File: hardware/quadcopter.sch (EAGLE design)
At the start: 55 parts, among them J1 HEADER-4POS-0.1IN-FEMALE-SMD-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, J2 HEADER-10POSTH-254X10, J3 HEADER-4POS-0.1IN-FEMALE, J4 AVR_SPI_PRG_6-SMD, M1 MOTOR_PADS_GND-MOLEX-SMD, M2 MOTOR_PADS_GND-MOLEX-SMD, M3 MOTOR_PADS_GND-MOLEX-SMD, M4 MOTOR_PADS_GND-MOLEX-SMD, Q1 N-MOSFET-SI2302DS, Q2 N-MOSFET-SI2302DS, Q3 N-MOSFET-SI2302DS, Q4 N-MOSFET-SI2302DS, SW1 PUSHBUTTON_-4.5X4.5, U1 ATMEGA128RFA1, U2 IMU_LSM9DS1-LSM9DS1, Y1 CRYSTAL5X3

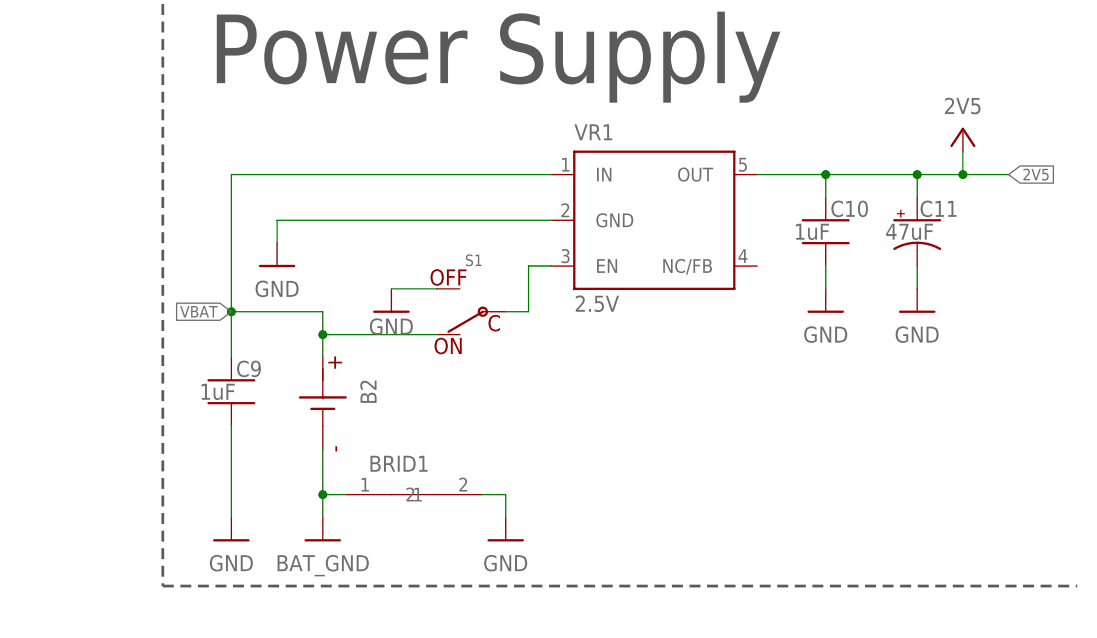
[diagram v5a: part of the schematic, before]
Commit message: Attempt to fix power supply to pass quick check
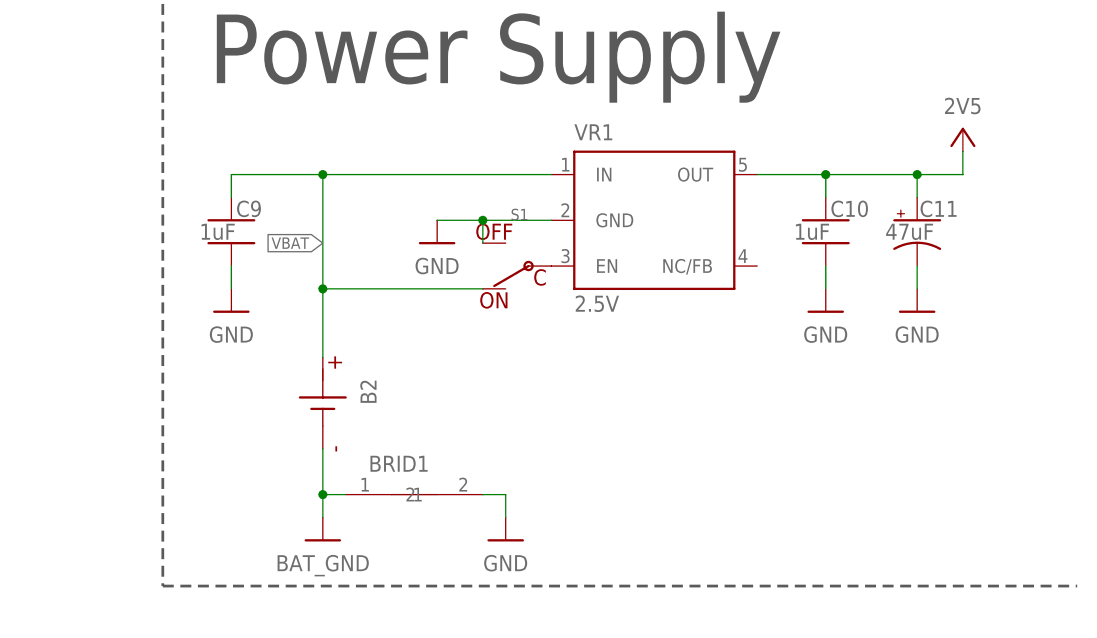
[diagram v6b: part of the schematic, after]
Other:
- moved on the sheet: C9, S1
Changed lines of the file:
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@@
 <part name="C10" library="quadparts_prebuilt_2022" library_urn="urn:adsk.wipprod:fs.file:vf.VudH_-qgS-enOFMGlZoxrw" deviceset="CAPACITOR-NP_" device="SMD-2012-0805_CERAMIC-1UF" value="1uF"/>
 <part name="S1" library="quadparts_prebuilt_2022" library_urn="urn:adsk.wipprod:fs.file:vf.VudH_-qgS-enOFMGlZoxrw" deviceset="POWER-SWITCH-MFS201N-9-Z" device="-SMD-EDGE"/>
-<part name="GND28" library="quadparts_prebuilt_2022" library_urn="urn:adsk.wipprod:fs.file:vf.VudH_-qgS-enOFMGlZoxrw" deviceset="GND" device=""/>
 <part name="GND31" library="quadparts_prebuilt_2022" library_urn="urn:adsk.wipprod:fs.file:vf.VudH_-qgS-enOFMGlZoxrw" deviceset="GND" device=""/>
 <part name="GND33" library="quadparts_prebuilt_2022" library_urn="urn:adsk.wipprod:fs.file:vf.VudH_-qgS-enOFMGlZoxrw" deviceset="GND" device=""/>
@@
 <attribute name="NAME" x="373.38" y="110.49" size="1.778" layer="95"/>
 </instance>
-<instance part="GND27" gate="1" x="340.36" y="96.52" smashed="yes">
-<attribute name="VALUE" x="340.36" y="93.98" size="1.778" layer="96" align="center"/>
-</instance>
-<instance part="C9" gate="G$1" x="335.28" y="83.82" smashed="yes">
-<attribute name="VALUE" x="331.724" y="81.661" size="1.778" layer="96"/>
-<attribute name="NAME" x="335.788" y="84.201" size="1.778" layer="95"/>
+<instance part="GND27" gate="1" x="358.14" y="99.06" smashed="yes">
+<attribute name="VALUE" x="358.14" y="96.52" size="1.778" layer="96" align="center"/>
+</instance>
+<instance part="C9" gate="G$1" x="335.28" y="101.6" smashed="yes">
+<attribute name="VALUE" x="331.724" y="99.441" size="1.778" layer="96"/>
+<attribute name="NAME" x="335.788" y="101.981" size="1.778" layer="95"/>
 </instance>
 <instance part="C10" gate="G$1" x="401.32" y="101.6" smashed="yes">
@@
 <attribute name="NAME" x="401.828" y="101.981" size="1.778" layer="95"/>
 </instance>
-<instance part="S1" gate="G$1" x="360.68" y="91.44" smashed="yes" rot="R180">
-<attribute name="NAME" x="363.22" y="97.79" size="1.27" layer="95" rot="R180"/>
-</instance>
-<instance part="GND28" gate="1" x="353.06" y="91.44" smashed="yes">
-<attribute name="VALUE" x="353.06" y="88.9" size="1.778" layer="96" align="bottom-center"/>
-</instance>
-<instance part="GND31" gate="1" x="335.28" y="66.04" smashed="yes">
-<attribute name="VALUE" x="335.28" y="63.5" size="1.778" layer="96" align="center"/>
+<instance part="S1" gate="G$1" x="365.76" y="96.52" smashed="yes" rot="R180">
+<attribute name="NAME" x="368.3" y="102.87" size="1.27" layer="95" rot="R180"/>
+</instance>
+<instance part="GND31" gate="1" x="335.28" y="91.44" smashed="yes">
+<attribute name="VALUE" x="335.28" y="88.9" size="1.778" layer="96" align="center"/>
 </instance>
 <instance part="GND33" gate="1" x="365.76" y="66.04" smashed="yes">
@@
 </segment>
 <segment>
-<wire x1="370.84" y1="101.6" x2="340.36" y2="101.6" width="0.1524" layer="91"/>
-<wire x1="340.36" y1="101.6" x2="340.36" y2="99.06" width="0.1524" layer="91"/>
+<wire x1="370.84" y1="101.6" x2="363.22" y2="101.6" width="0.1524" layer="91"/>
+<wire x1="363.22" y1="101.6" x2="358.14" y2="101.6" width="0.1524" layer="91"/>
 <pinref part="VR1" gate="G$1" pin="GND"/>
 <pinref part="GND27" gate="1" pin="GND"/>
-</segment>
-<segment>
 <pinref part="S1" gate="G$1" pin="OFF"/>
-<pinref part="GND28" gate="1" pin="GND"/>
-<wire x1="353.06" y1="93.98" x2="358.14" y2="93.98" width="0.1524" layer="91"/>
-</segment>
-<segment>
-<wire x1="335.28" y1="78.74" x2="335.28" y2="68.58" width="0.1524" layer="91"/>
+<wire x1="363.22" y1="99.06" x2="363.22" y2="101.6" width="0.1524" layer="91"/>
+<junction x="363.22" y="101.6"/>
+</segment>
+<segment>
+<wire x1="335.28" y1="96.52" x2="335.28" y2="93.98" width="0.1524" layer="91"/>
 <pinref part="C9" gate="G$1" pin="2"/>
 <pinref part="GND31" gate="1" pin="GND"/>
@@
 </segment>
 <segment>
-<wire x1="358.14" y1="88.9" x2="345.44" y2="88.9" width="0.1524" layer="91"/>
-<wire x1="345.44" y1="91.44" x2="345.44" y2="88.9" width="0.1524" layer="91"/>
-<wire x1="345.44" y1="88.9" x2="345.44" y2="86.36" width="0.1524" layer="91"/>
-<label x="335.28" y="91.44" size="1.27" layer="95" font="vector" rot="MR0" xref="yes"/>
-<wire x1="345.44" y1="91.44" x2="335.28" y2="91.44" width="0.1524" layer="91"/>
-<wire x1="370.84" y1="106.68" x2="335.28" y2="106.68" width="0.1524" layer="91"/>
-<wire x1="335.28" y1="106.68" x2="335.28" y2="91.44" width="0.1524" layer="91"/>
-<wire x1="335.28" y1="91.44" x2="335.28" y2="86.36" width="0.1524" layer="91"/>
+<wire x1="363.22" y1="93.98" x2="345.44" y2="93.98" width="0.1524" layer="91"/>
+<wire x1="345.44" y1="106.68" x2="345.44" y2="93.98" width="0.1524" layer="91"/>
+<wire x1="345.44" y1="93.98" x2="345.44" y2="86.36" width="0.1524" layer="91"/>
+<label x="345.44" y="99.06" size="1.27" layer="95" font="vector" rot="MR0" xref="yes"/>
+<wire x1="345.44" y1="106.68" x2="335.28" y2="106.68" width="0.1524" layer="91"/>
+<wire x1="370.84" y1="106.68" x2="345.44" y2="106.68" width="0.1524" layer="91"/>
+<wire x1="335.28" y1="106.68" x2="335.28" y2="104.14" width="0.1524" layer="91"/>
 <pinref part="B2" gate="G$1" pin="P"/>
 <pinref part="VR1" gate="G$1" pin="IN"/>
 <pinref part="C9" gate="G$1" pin="1"/>
-<junction x="345.44" y="88.9"/>
-<junction x="335.28" y="91.44"/>
 <pinref part="S1" gate="G$1" pin="ON"/>
+<junction x="345.44" y="93.98"/>
+<junction x="345.44" y="106.68"/>
 </segment>
 <segment>
@@
 <wire x1="401.32" y1="106.68" x2="401.32" y2="104.14" width="0.1524" layer="91"/>
 <wire x1="401.32" y1="106.68" x2="411.48" y2="106.68" width="0.1524" layer="91"/>
-<label x="421.64" y="106.68" size="1.27" layer="95" font="vector" xref="yes"/>
 <wire x1="411.48" y1="106.68" x2="416.56" y2="106.68" width="0.1524" layer="91"/>
 <wire x1="411.48" y1="104.14" x2="411.48" y2="106.68" width="0.1524" layer="91"/>
-<junction x="416.56" y="106.68"/>
 <junction x="401.32" y="106.68"/>
 <junction x="411.48" y="106.68"/>
-<wire x1="416.56" y1="106.68" x2="421.64" y2="106.68" width="0.1524" layer="91"/>
 <pinref part="P+5" gate="G$1" pin="2V5"/>
 <pinref part="VR1" gate="G$1" pin="OUT"/>
@@
 <net name="N$23" class="0">
 <segment>
-<wire x1="365.76" y1="91.44" x2="368.3" y2="91.44" width="0.1524" layer="91"/>
-<wire x1="368.3" y1="91.44" x2="368.3" y2="96.52" width="0.1524" layer="91"/>
-<wire x1="368.3" y1="96.52" x2="370.84" y2="96.52" width="0.1524" layer="91"/>
 <pinref part="VR1" gate="G$1" pin="EN"/>
 <pinref part="S1" gate="G$1" pin="C"/>

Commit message: Added LED library and sample ground effect LED to schematic
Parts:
- added D7: red, LED:LED-350-2312-1-ND-REVERSE
- added R8: 100, quadparts_prebuilt_2022:RESISTOR_SMD-2012-0805-100
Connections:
- new net N$17: D7.A, R8.2
- new net PG5: R8.1, U1.PG5(OC0B)
- net GND: now also D7.C
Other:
- note added: "Ground Effect LEDs"
- note added: "LEDs"
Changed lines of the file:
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@@
 <part name="U2" library="custom_michael_shao" deviceset="IMU_LSM9DS1" device="-LSM9DS1"/>
 <part name="BRID1" library="custom_michael_shao" deviceset="NET_BRIDGE" device="_5X5"/>
+<part name="R8" library="quadparts_prebuilt_2022" library_urn="urn:adsk.wipprod:fs.file:vf.VudH_-qgS-enOFMGlZoxrw" deviceset="RESISTOR_" device="SMD-2012-0805-100" value="100"/>
+<part name="D7" library="LED" deviceset="LED-350-2312-1-ND" device="-REVERSE" value="red"/>
+<part name="GND28" library="quadparts_prebuilt_2022" library_urn="urn:adsk.wipprod:fs.file:vf.VudH_-qgS-enOFMGlZoxrw" deviceset="GND" device=""/>
 </parts>
 <sheets>
@@
 <wire x1="154.94" y1="129.54" x2="327.66" y2="129.54" width="0.3048" layer="97" style="longdash"/>
 <text x="205.74" y="261.62" size="7.62" layer="97">Microcontroller</text>
+<wire x1="154.94" y1="129.54" x2="154.94" y2="86.36" width="0.3048" layer="97" style="longdash"/>
+<wire x1="154.94" y1="86.36" x2="154.94" y2="60.96" width="0.3048" layer="97" style="longdash"/>
+<wire x1="154.94" y1="60.96" x2="220.98" y2="60.96" width="0.3048" layer="97" style="longdash"/>
+<text x="157.48" y="127" size="6.35" layer="97" align="top-left">LEDs</text>
+<text x="157.48" y="63.5" size="3.175" layer="97">Ground Effect LEDs</text>
+<wire x1="220.98" y1="60.96" x2="327.66" y2="60.96" width="0.3048" layer="97" style="longdash"/>
+<wire x1="154.94" y1="86.36" x2="220.98" y2="86.36" width="0.1524" layer="97" style="longdash"/>
+<wire x1="220.98" y1="86.36" x2="220.98" y2="60.96" width="0.1524" layer="97" style="longdash"/>
 </plain>
 <instances>
@@
 <instance part="BRID1" gate="G$1" x="355.6" y="71.12" smashed="yes">
 <attribute name="NAME" x="350.52" y="73.66" size="1.778" layer="95"/>
+</instance>
+<instance part="R8" gate="G$1" x="172.72" y="76.2" smashed="yes">
+<attribute name="VALUE" x="168.91" y="72.898" size="1.778" layer="96"/>
+<attribute name="NAME" x="168.91" y="77.6986" size="1.778" layer="95"/>
+</instance>
+<instance part="D7" gate="G$1" x="180.34" y="76.2" smashed="yes">
+<attribute name="NAME" x="177.292" y="77.978" size="1.778" layer="95"/>
+<attribute name="VALUE" x="177.038" y="70.993" size="1.778" layer="96"/>
+</instance>
+<instance part="GND28" gate="1" x="187.96" y="73.66" smashed="yes">
+<attribute name="VALUE" x="187.96" y="71.12" size="1.778" layer="96" align="center"/>
 </instance>
 </instances>
@@
 <pinref part="GND30" gate="1" pin="GND"/>
 <pinref part="C11" gate="G$1" pin="-"/>
+</segment>
+<segment>
+<pinref part="GND28" gate="1" pin="GND"/>
+<wire x1="187.96" y1="76.2" x2="185.42" y2="76.2" width="0.1524" layer="91"/>
+<pinref part="D7" gate="G$1" pin="C"/>
 </segment>
 </net>
@@
 </segment>
 </net>
+<net name="N$17" class="0">
+<segment>
+<pinref part="R8" gate="G$1" pin="2"/>
+<pinref part="D7" gate="G$1" pin="A"/>
+</segment>
+</net>
+<net name="PG5" class="0">
+<segment>
+<pinref part="R8" gate="G$1" pin="1"/>
+<wire x1="167.64" y1="76.2" x2="165.1" y2="76.2" width="0.1524" layer="91"/>
+<label x="165.1" y="76.2" size="1.27" layer="95" rot="R180" xref="yes"/>
+</segment>
+<segment>
+<pinref part="U1" gate="G$1" pin="PG5(OC0B)"/>
+<wire x1="185.42" y1="139.7" x2="182.88" y2="139.7" width="0.1524" layer="91"/>
+<label x="182.88" y="139.7" size="1.27" layer="95" rot="R180" xref="yes"/>
+</segment>
+</net>
